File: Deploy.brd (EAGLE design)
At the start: 30 x 60 mm, 32 parts, among them SW5 THAU13-AB-R, SW6 THAU13-AB-R, SW7 TVAF06-A020B-R, SW8 TVAF06-A020B-R, U4 OPA340N, U5 DRIVER-LV8548MC-AH(SOIC10), U6 I-02247_NJM2845

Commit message: Deploy unit
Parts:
- added FET1, FET2: FDS4935A, mosfets:SOIC127P600X175-8N
- added RN1, RN2, RN3: 10k, resistor-dil:4X0402ARV341
- added T2, T3: HN1C01FU, transistors:SOT-363
- renumbered LED4 to LED2, LED5 to LED1, LED6 to LED3
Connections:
- removed net I2C_SCL: U$2.IO22
- removed net I2C_SDA: U$2.IO21
- removed net SPI_CLK: U$2.IO18
- removed net SPI_CS: U$2.IO5
- removed net SPI_MISO: U$2.IO19
- new net C1: RN3.1, U$2.IO21
- new net C2: RN3.2, U$2.IO19
- new net C3: RN3.3, U$2.IO18
- new net C4: RN3.4, U$2.IO5
- new net D1: FET1.5, FET1.6
- new net D2: FET1.7, FET1.8
- new net D3: FET2.5, FET2.6
- new net D4: FET2.7, FET2.8
- new net N$1: FET1.4, RN1.5, T2.6
- new net N$13: FET2.4, RN2.5, T3.6
- new net N$14: FET2.2, RN2.8, T3.3
- new net N$15: RN2.6, RN3.5, T3.5
- new net N$2: FET1.2, RN1.8, T2.3
- new net N$3: RN1.7, RN3.8, T2.2
- new net N$4: RN1.6, RN3.7, T2.5
- new net N$7: RN2.7, RN3.6, T3.2
- new net S1: U$2.SENSOR_VP
- new net S2: U$2.SENSOR_VN
- new net S3: U$2.IO34
- new net S4: U$2.IO23
- net GND: now also RN1.2, RN1.3, RN2.2, RN2.3, T2.1, T2.4, T3.1, T3.4
- net VCC: now also FET1.1, FET1.3, FET2.1, FET2.3, RN1.1, RN1.4, RN2.1, RN2.4
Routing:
- net VCC: track 27.8 -> 85.8 mm, vias 0 -> 6
- net GND: track 222.8 -> 265.3 mm, vias 11 -> 17
- net D3: track 0.00 -> 24.3 mm, vias 0 -> 1
- net S2: track 0.00 -> 19.6 mm, vias 0 -> 2
- net S3: track 0.00 -> 17.5 mm, vias 0 -> 2
- net D4: track 0.00 -> 17.3 mm, vias 0 -> 1
- net S1: track 0.00 -> 17.0 mm, vias 0 -> 2
- net D1: track 0.00 -> 15.1 mm, vias 0 -> 1
- net N$3: track 0.00 -> 13.5 mm
- net N$15: track 0.00 -> 10.9 mm
- net N$7: track 0.00 -> 9.57 mm
- net D2: track 0.00 -> 9.51 mm, vias 0 -> 1
- net N$2: track 0.00 -> 7.82 mm
- net N$14: track 0.00 -> 7.82 mm
- net N$13: track 0.00 -> 7.77 mm
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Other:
- board text added: "D1"
- board text added: "D2"
- board text added: "D3"
- board text added: "D4"
- board text added: "GND"
- board text added: "S1"
- board text added: "S2"
- board text added: "S3"
- board text added: "S4"

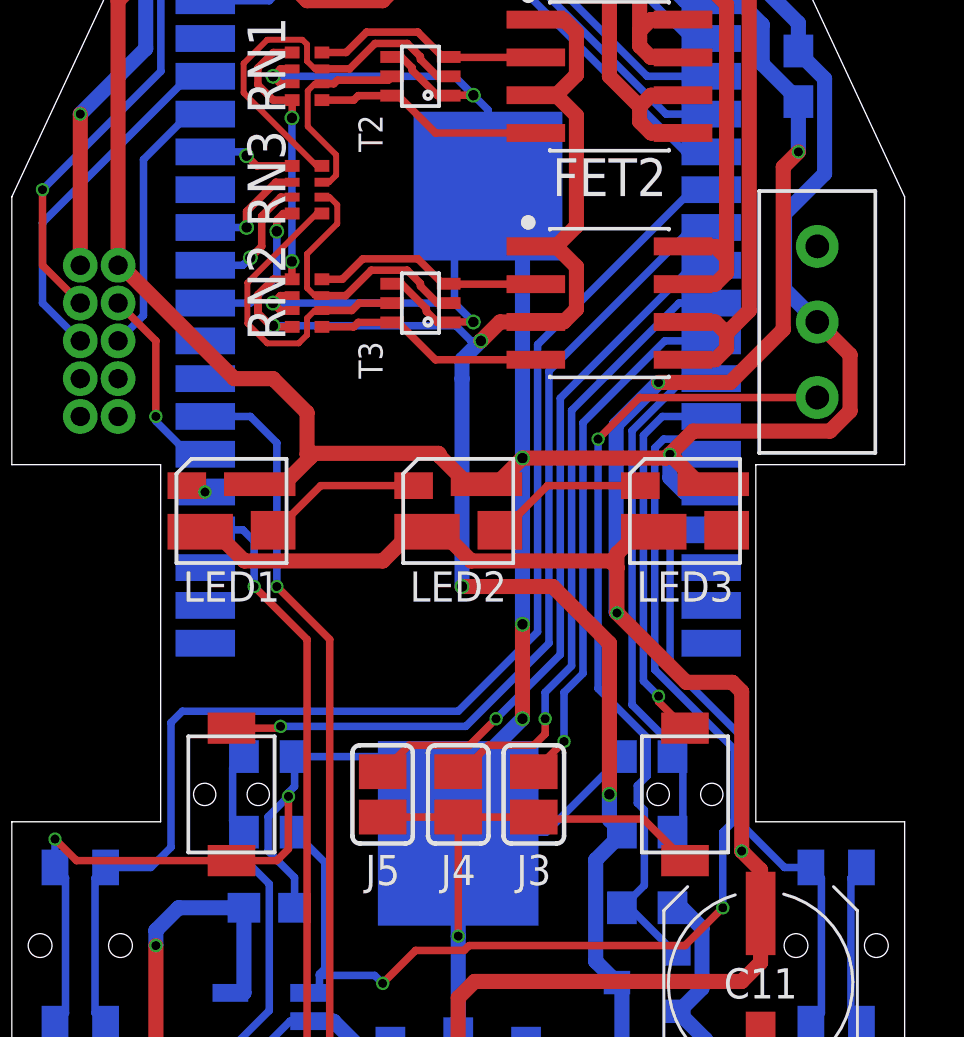
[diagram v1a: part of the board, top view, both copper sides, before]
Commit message: Fix analog input pins
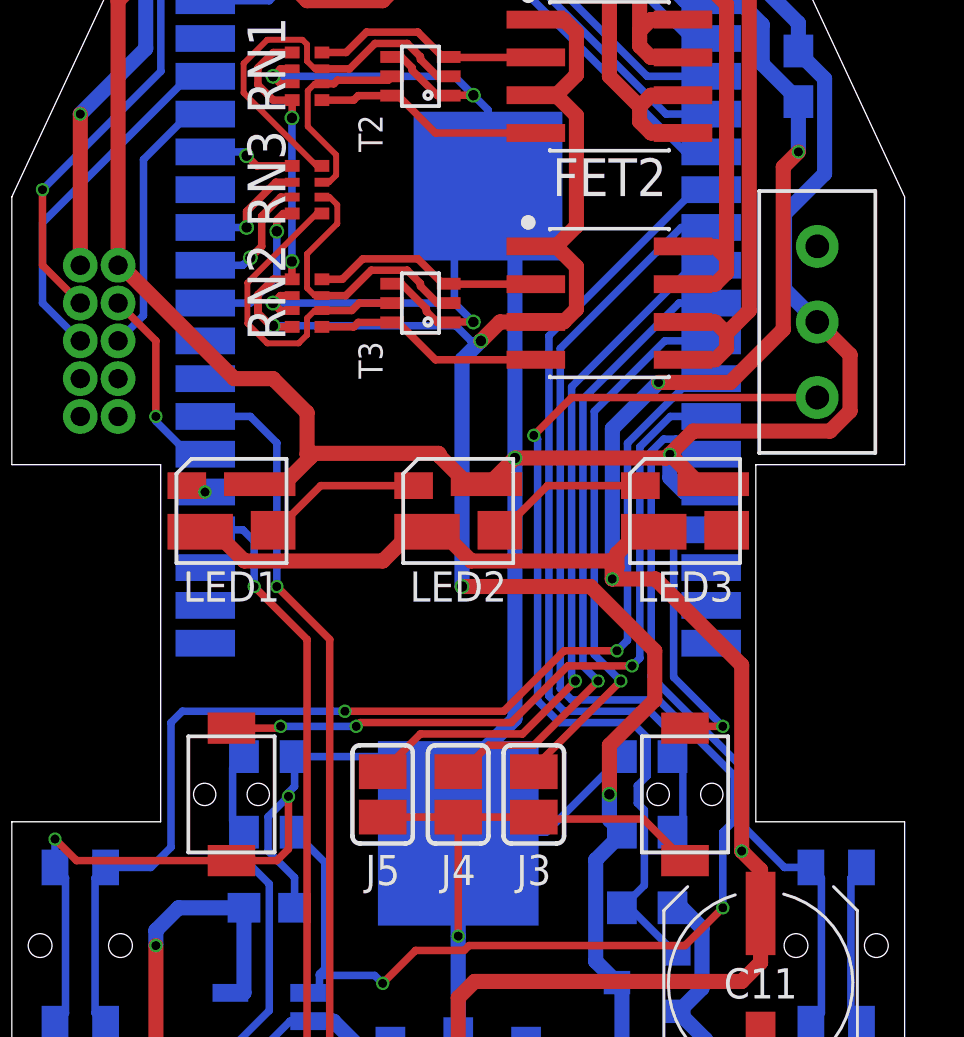
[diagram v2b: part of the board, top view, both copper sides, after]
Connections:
- net MSENSE: now also U$2.IO32; no longer U$2.IO12
- net SW1: now also U$2.IO12; no longer U$2.IO13
- net SW2: now also U$2.IO27; no longer U$2.IO35
- net SW3: now also U$2.IO13; no longer U$2.IO14
- net SW4: now also U$2.IO14; no longer U$2.IO32
- net VSENSE: now also U$2.IO35; no longer U$2.IO27
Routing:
- net MSENSE: track 39.9 -> 50.8 mm
- net VSENSE: track 17.7 -> 27.9 mm
- net N$10: track 27.4 -> 32.0 mm
- net SW2: track 43.4 -> 39.0 mm, vias 0 -> 2
- net SW1: track 20.5 -> 24.7 mm
- net SW4: track 28.4 -> 24.6 mm, vias 1 -> 3
- net SW3: track 13.0 -> 9.62 mm
- net VCC: track 85.8 -> 87.8 mm
- net J2: track 23.1 -> 24.1 mm
- net VDD: track 133.1 -> 132.3 mm
- net J0: track 17.9 -> 18.6 mm
- net GND: track 265.3 -> 265.0 mm, vias 17 -> 15

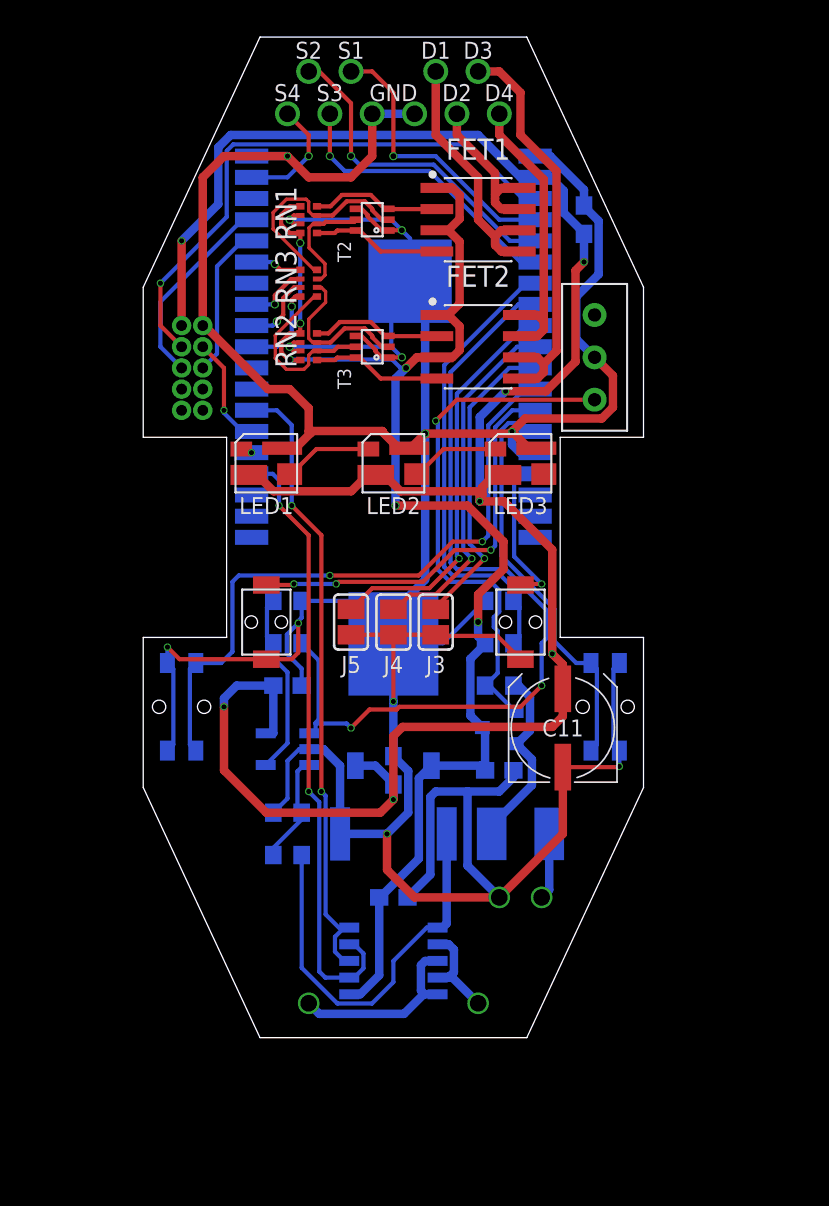
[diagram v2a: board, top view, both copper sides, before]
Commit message: reduce switch pins
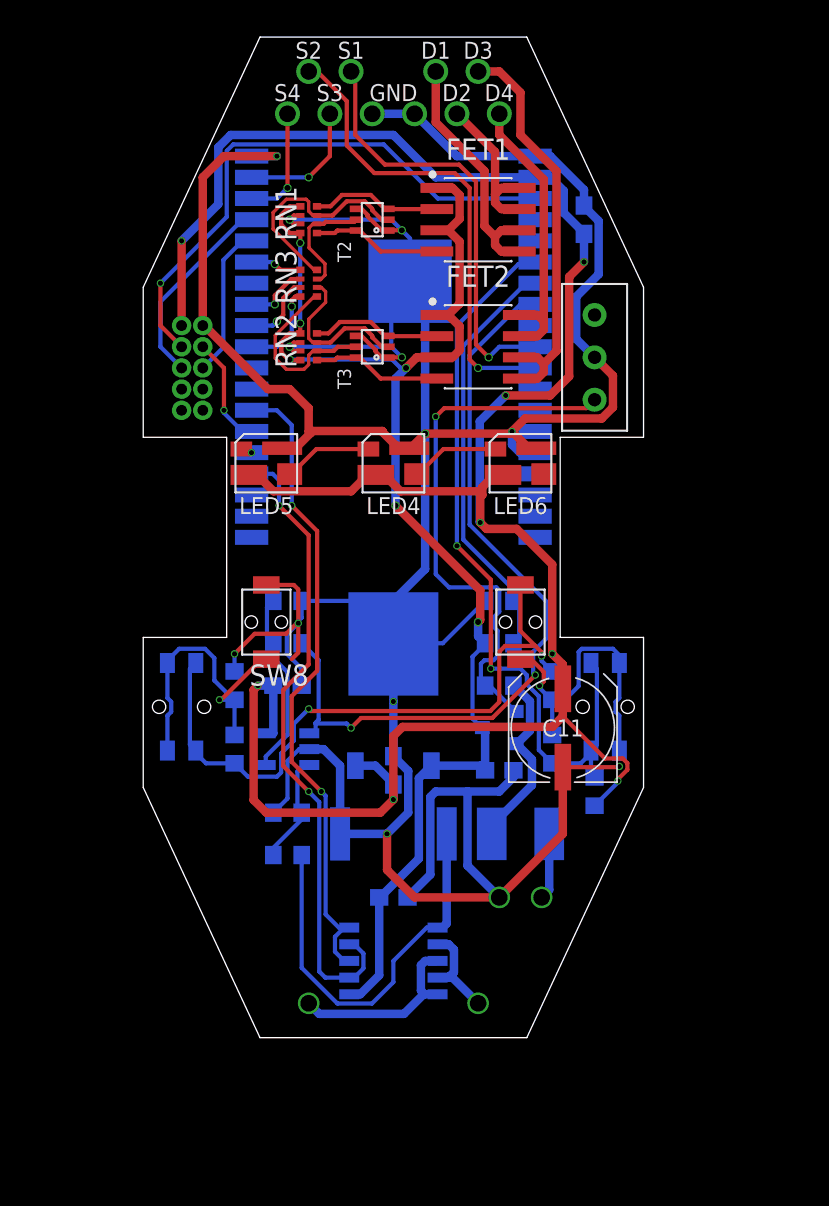
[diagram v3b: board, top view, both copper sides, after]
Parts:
- removed J3, J4, J5: (no value), jumper:SJ
- removed R8: 1k, rcl:R0603
- removed R9: 100k, rcl:R0603
- added R18, R19: 100k, rcl:R0603
- added R20, R21, R22, R23, R24: (no value), rcl:R0603
- R13: value 100k -> 1k
- moved R14 13.0 mm to (-6.35, -6.35)
- moved R13 12.7 mm to (-6.35, -3.81), turned to 0 degrees
- turned SW7 to 180 degrees
- turned SW8 to 180 degrees
- renumbered LED1 to LED5, LED2 to LED4, LED3 to LED6, R10 to R15, R11 to R16, R12 to R17
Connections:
- removed net J0: J3.1, U$2.IO26
- removed net J1: J4.1, U$2.IO25
- removed net J2: J5.1, U$2.IO33
- removed net N$10: R14.1, T1.3, U$4.1
- removed net N$5: HUSE1.2, R14.2, T1.2
- removed net N$8: R8.2, R9.1, U4.4
- removed net SW1: SW6.1, SW6.2, U$2.IO12
- removed net SW2: SW5.1, SW5.2, U$2.IO27
- removed net SW3: SW7.P$1, U$2.IO13
- removed net SW4: SW8.P$1, U$2.IO14
- new net N$18: HUSE1.2, R19.2, T1.2
- new net N$19: R13.2, R14.1, U4.4
- new net N$21: R19.1, T1.3, U$4.1
- new net N$24: R22.1, R23.2, SW5.1, SW5.2, SW7.P$2
- new net N$25: R21.1, R22.2, SW6.3, SW6.4, SW7.P$1
- new net N$26: R23.1, R24.2, SW5.3, SW5.4, SW8.P$1
- new net SW: R20.1, R21.2, SW6.1, SW6.2, U$2.IO34
- net GND: now also R18.1, R24.1; no longer J3.2, J4.2, J5.2, R8.1, SW5.3, SW5.4, SW6.3, SW6.4, SW7.P$2
- net MSENSE: now also R14.2; no longer R9.2
- net S1: now also U$2.IO25; no longer U$2.SENSOR_VP
- net S2: now also U$2.IO26; no longer U$2.SENSOR_VN
- net S3: now also U$2.IO23; no longer U$2.IO34
- net S4: now also U$2.IO22; no longer U$2.IO23
- net VDD: now also R20.2
- net VSENSE: now also R18.2; no longer R13.2
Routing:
- net SW: track 0.00 -> 45.9 mm, vias 0 -> 2
- net SW2: track 39.0 -> 0.00 mm, vias 2 -> 0
- net N$24: track 0.00 -> 39.0 mm, vias 0 -> 2
- net N$21: track 0.00 -> 32.9 mm, vias 0 -> 1
- net N$10: track 32.0 -> 0.00 mm, vias 1 -> 0
- net GND: track 265.0 -> 235.9 mm
- net SW1: track 24.7 -> 0.00 mm
- net SW4: track 24.6 -> 0.00 mm, vias 3 -> 0
- net J2: track 24.1 -> 0.00 mm, vias 1 -> 0
- net J1: track 21.3 -> 0.00 mm, vias 1 -> 0
- net N$26: track 0.00 -> 18.8 mm, vias 0 -> 1
- net J0: track 18.6 -> 0.00 mm, vias 1 -> 0
- net N$25: track 0.00 -> 18.5 mm, vias 0 -> 1
- net N$8: track 11.6 -> 0.00 mm
- net N$19: track 0.00 -> 11.6 mm
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
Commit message: change parts name
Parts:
- removed R24: (no value), rcl:R0603
- added R6: 1k, rcl:R0603
- R13: value 1k -> (none)
- moved R13 5.99 mm to (-9.53, -8.89), turned to 270 degrees
- renumbered C10 to C2, C11 to C3, C12 to C4, C7 to C6, C8 to C5, C9 to C1, R14 to R8, R15 to R4, R16 to R7, R17 to R2, R18 to R3, R19 to R1, R20 to R9, R21 to R10, R22 to R11, R23 to R12, RS1 to R5
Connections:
- net GND: now also R6.1; no longer R24.1
- net N$19: now also R6.2; no longer R13.2
- net N$26: now also R13.2; no longer R24.2

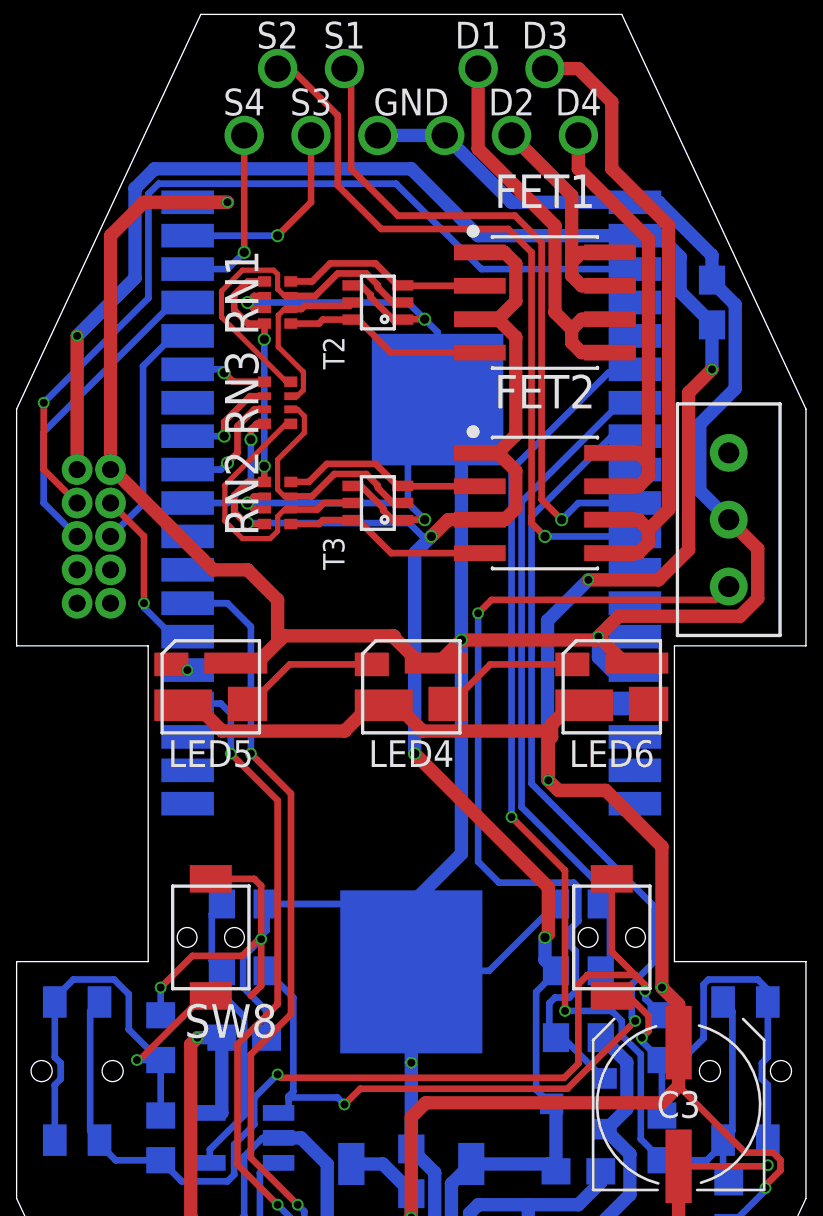
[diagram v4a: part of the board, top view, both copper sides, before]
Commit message: Format silk
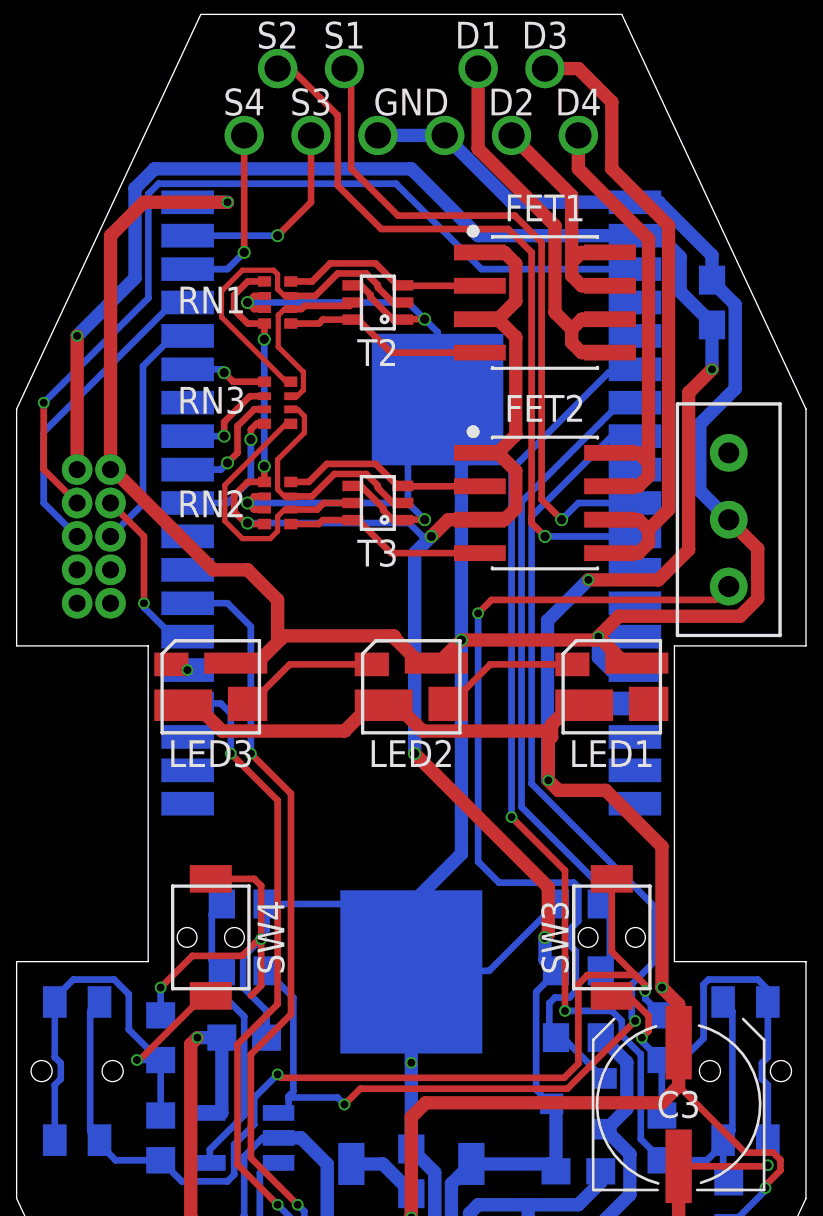
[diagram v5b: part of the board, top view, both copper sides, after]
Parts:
- renumbered LED4 to LED2, LED5 to LED3, LED6 to LED1, SW5 to SW2, SW6 to SW1, SW7 to SW3, SW8 to SW4

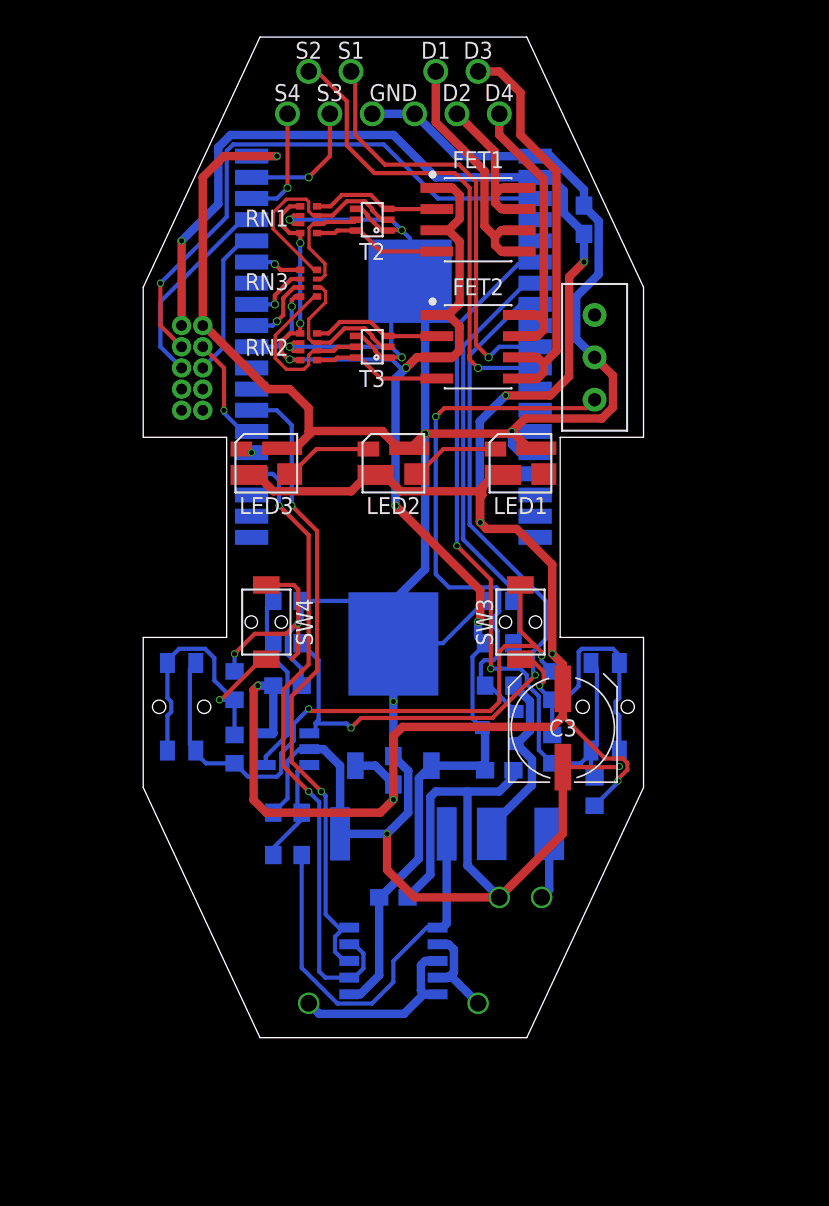
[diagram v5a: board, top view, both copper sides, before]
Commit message: Add GND plane
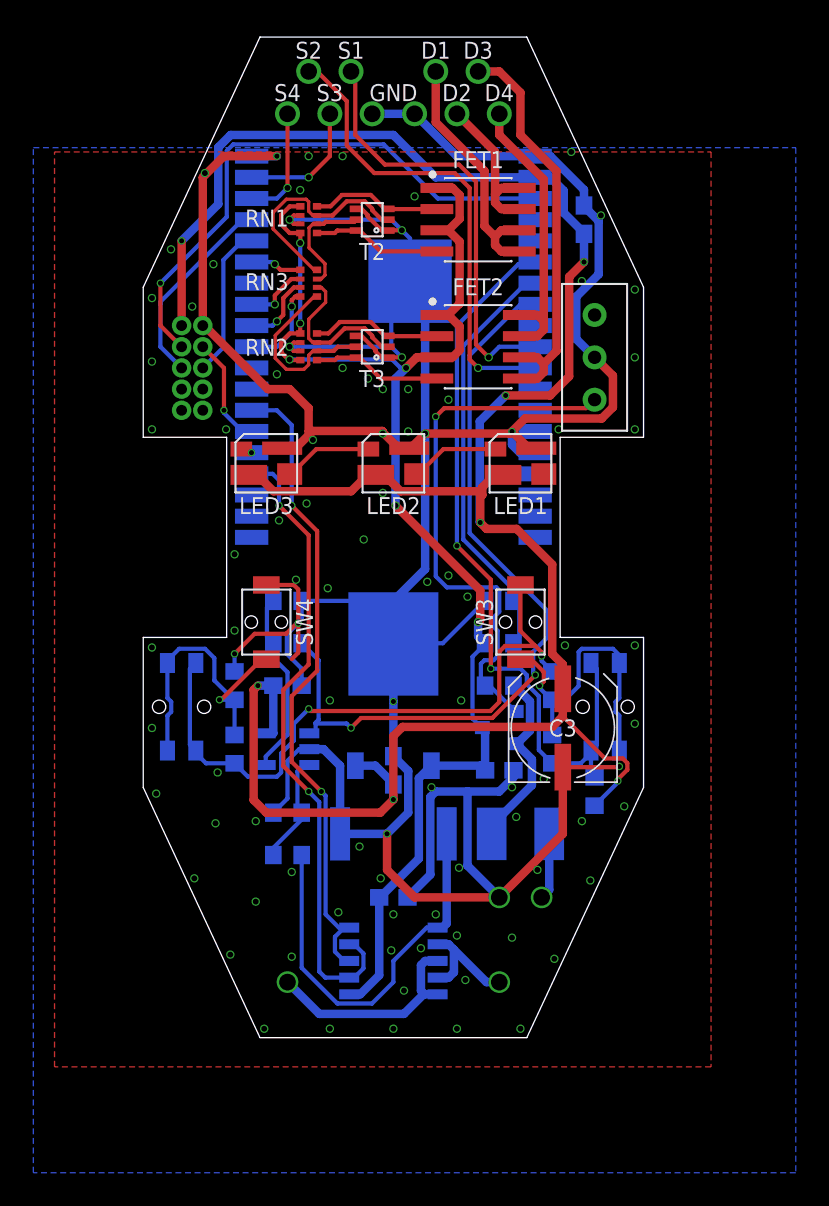
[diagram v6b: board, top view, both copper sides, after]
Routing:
- net M1: track 11.4 -> 13.2 mm
- net M2: track 5.93 -> 7.11 mm
- net VDD: vias 8 -> 7
- net GND: vias 15 -> 96
- added copper zone on layer 1, net GND
- added copper zone on layer 16, net GND
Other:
- board text added: "2022 WASA Rocket"
